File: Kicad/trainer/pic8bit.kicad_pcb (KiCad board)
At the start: 2 copper layers, 160 x 100 mm, 119 parts, among them K101 AC/DC 9-12V, K102 AC/DC 9-12V, K103 PE-450-4X6X-BLACK, K201 MCU 1, K202 MCU 2, K203 ICSP, K204 VIN, K205 VIN, K206 VDD, K207 GND, K208 VDD, K209 GND, K210 HARWIN-254-F-1X10-VERTICAL, K301 I2C/GPIO, K302 I2C/SPI, K303 SPI/GPIO, K304 EUSART/TTL, K401 HARWIN-254-F-1X10-VERTICAL, K402 HARWIN-254-F-1X10-VERTICAL, K409 HARWIN-254-F-1X16-VERTICAL, P401 AN1, P402 AN2, U101 KEYSTONE-24283, U102 KEYSTONE-24283, U103 KEYSTONE-24283, U104 KEYSTONE-24283, U105 NCP5662-ADJ, U201 PIC16F/18F, X101 3M-SJ5376, X102 3M-SJ5376, X103 3M-SJ5376, X104 3M-SJ5376, X105 3M-SJ5376, X201 XTAL-DIL08

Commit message: Up
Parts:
- R401: footprint tronixio:PIHER-PT10LV -> tronixio:PIHER-PT10MV
- U101, U102, U103, U104: value KEYSTONE-24283 -> 24283
- U201: footprint tronixio:DIP-28-W762-SOCKET -> tronixio:DIP-28-W762
- moved S201 0.81 mm to (191.0, 142.0)
- turned S403 to 180 degrees
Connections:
- net VDD renamed +VDD
- net VIN renamed +VIN
- S403 pad 4: GND -> /HID/S5
- S403 pad 5: /HID/S5 -> GND
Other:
- board text removed: "Reset"

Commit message: Up
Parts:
- moved S101 0.25 mm to (88.8, 51.0)
- moved R101 0.20 mm to (103.5, 50.8)
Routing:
- net /HID/S4: track 64.3 -> 65.0 mm
- net /HID/S3: track 85.3 -> 86.0 mm
- net /HID/S1: track 125.4 -> 126.1 mm
- net /HID/S2: track 105.4 -> 106.2 mm
- net /HID/A: track 40.0 -> 40.7 mm
- net Net-(JP401-Pad1): track 15.7 -> 16.4 mm
- net /HID/B: track 37.5 -> 38.2 mm

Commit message: Update
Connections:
- X201 pad 2: GND -> unconnected-(X201-Pad2)
- X201 pad 4: Net-(K201-Pin_9) -> unconnected-(X201-Pad4)
- X201 pad 6: Net-(K201-Pin_10) -> unconnected-(X201-Pad6)
- X201 pad 7: GND -> unconnected-(X201-Pad7)
- X201 pad 8: GND -> unconnected-(X201-Pad8)

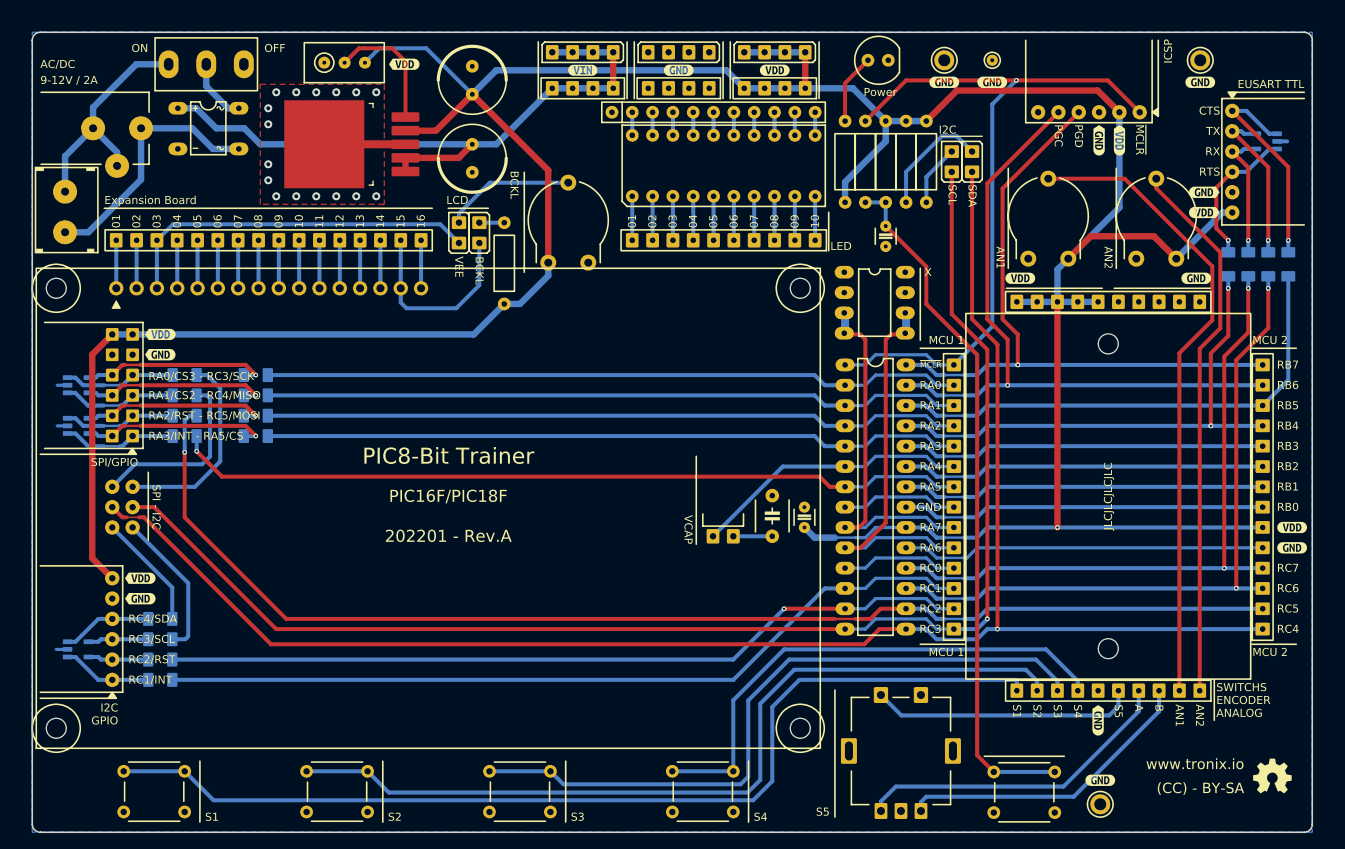
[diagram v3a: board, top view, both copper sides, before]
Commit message: Update Trainer Kicad 8
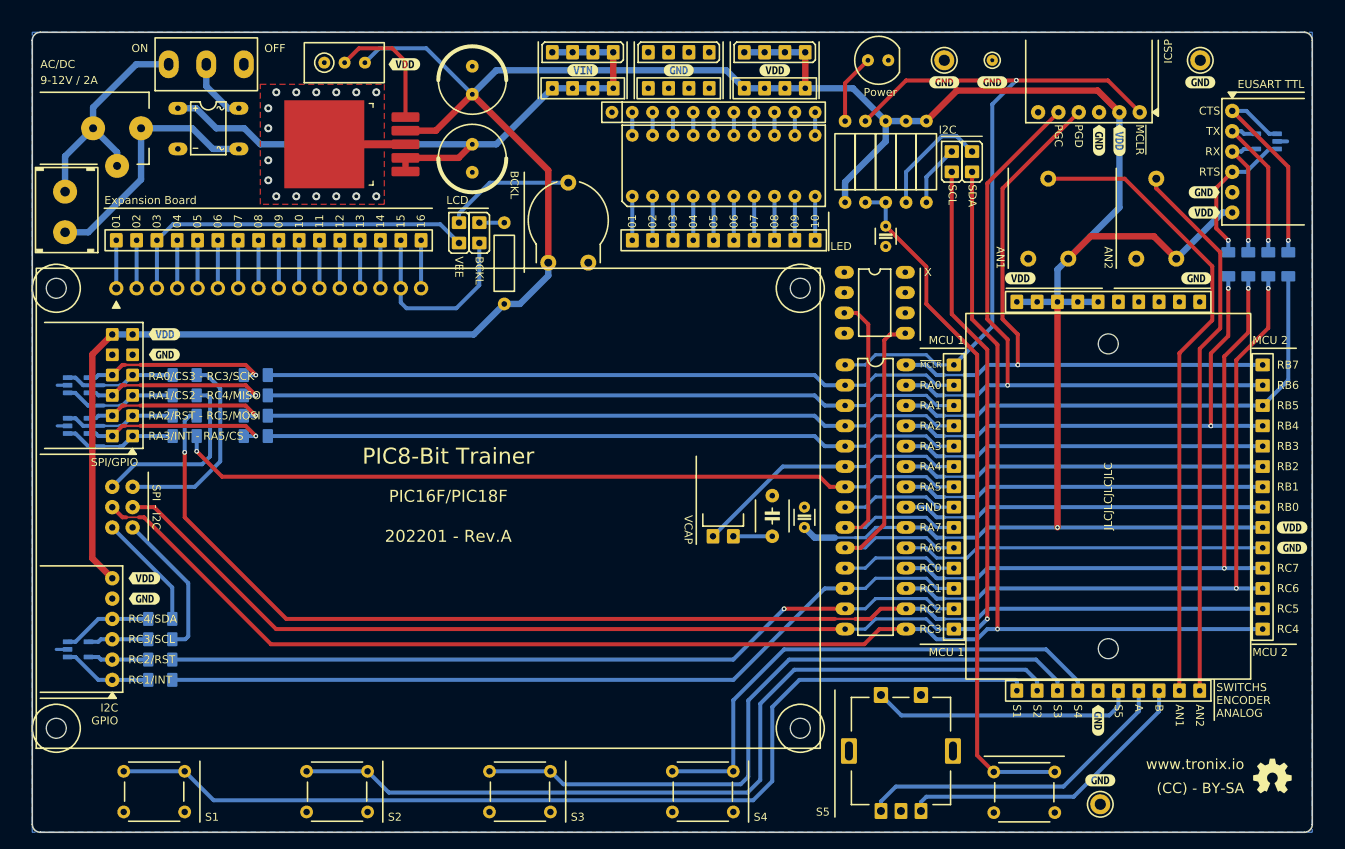
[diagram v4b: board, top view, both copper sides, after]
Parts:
- removed kibuzzard-62A777FA (x7): G***, kibuzzard-62A777FA
- removed kibuzzard-62A77857: G***, kibuzzard-62A77857
- removed kibuzzard-62A778D1 (x2): G***, kibuzzard-62A778D1
- removed kibuzzard-62A778F0: G***, kibuzzard-62A778F0
- removed kibuzzard-62A77FCE: G***, kibuzzard-62A77FCE
- removed kibuzzard-62A77FF4: G***, kibuzzard-62A77FF4
- removed kibuzzard-62A78037: G***, kibuzzard-62A78037
- removed kibuzzard-62A78078: G***, kibuzzard-62A78078
- removed kibuzzard-62A780A0 (x2): G***, kibuzzard-62A780A0
- removed kibuzzard-62A780B6: G***, kibuzzard-62A780B6
- removed kibuzzard-62AA3F24: G***, kibuzzard-62AA3F24
- removed kibuzzard-62ACBAD0: G***, kibuzzard-62ACBAD0
- removed kibuzzard-62ACDA78: G***, kibuzzard-62ACDA78
- added kibuzzard-65F60515: G***, kibuzzard-65F60515, F.Cu at (113.5, 51.0)
- added kibuzzard-65F60520: G***, kibuzzard-65F60520, F.Cu at (135.8, 51.8)
- added kibuzzard-65F6052C: G***, kibuzzard-65F6052C, F.Cu at (147.8, 51.8)
- added kibuzzard-65F60537: G***, kibuzzard-65F60537, F.Cu at (159.8, 51.8)
- added kibuzzard-65F60546: G***, kibuzzard-65F60546, F.Cu at (181.0, 53.2)
- added kibuzzard-65F60553: G***, kibuzzard-65F60553, F.Cu at (187.0, 53.2)
- added kibuzzard-65F60562: G***, kibuzzard-65F60562, F.Cu at (200.3, 60.5)
- added kibuzzard-65F6056F: G***, kibuzzard-65F6056F, F.Cu at (202.9, 60.5)
- added kibuzzard-65F60578: G***, kibuzzard-65F60578, F.Cu at (213.0, 53.2)
- added kibuzzard-65F60585: G***, kibuzzard-65F60585, F.Cu at (213.5, 67.0)
- added kibuzzard-65F60590: G***, kibuzzard-65F60590, F.Cu at (213.5, 69.5)
- added kibuzzard-65F6059C: G***, kibuzzard-65F6059C, F.Cu at (212.5, 77.8)
- added kibuzzard-65F605A7: G***, kibuzzard-65F605A7, F.Cu at (190.5, 77.8)
- added kibuzzard-65F605B3: G***, kibuzzard-65F605B3, F.Cu at (224.5, 108.9)
- added kibuzzard-65F605BE: G***, kibuzzard-65F605BE, F.Cu at (224.5, 111.4)
- added kibuzzard-65F605CA: G***, kibuzzard-65F605CA, F.Cu at (200.2, 133.0)
- added kibuzzard-65F605D7: G***, kibuzzard-65F605D7, F.Cu at (200.5, 140.5)
- added kibuzzard-65F605E6: G***, kibuzzard-65F605E6, F.Cu at (81.0, 117.8)
- added kibuzzard-65F605F2: G***, kibuzzard-65F605F2, F.Cu at (81.0, 115.2)
- added kibuzzard-65F60603: G***, kibuzzard-65F60603, F.Cu at (83.5, 87.3)
- added kibuzzard-65F60610: G***, kibuzzard-65F60610, F.Cu at (83.5, 84.8)
- LED101: footprint tronixio:LED-TH-05MM -> tronixio:LED-TH-ROUND-05MM
- U101, U102, U103, U104: value 24283 -> KEYSTONE-24283
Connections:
- net +VDD renamed POWER-VDD
- net +VIN renamed POWER-VIN
- net GND renamed POWER-GND
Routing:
- net Net-(K201-Pin_10): track 49.3 -> 46.8 mm

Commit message: Update Trainer
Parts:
- moved kibuzzard-65F60515 0.25 mm to (113.8, 51.0)
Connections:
- X201 pad 2: unconnected-(X201-Pad2) -> POWER-GND
- X201 pad 4: unconnected-(X201-Pad4) -> Net-(K201-Pin_9)
- X201 pad 6: unconnected-(X201-Pad6) -> Net-(K201-Pin_10)
- X201 pad 7: unconnected-(X201-Pad7) -> POWER-GND
- X201 pad 8: unconnected-(X201-Pad8) -> POWER-GND
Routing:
- net POWER-GND: track 75.7 -> 70.4 mm
- net Net-(K201-Pin_10): track 46.8 -> 49.2 mm
- net POWER-VDD: track 405.2 -> 405.9 mm

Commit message: Update
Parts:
- U201: footprint tronixio:DIP-28-W762 -> tronixio:DIP-28-W762-SOCKET

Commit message: Up
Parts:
- U101, U102, U103, U104: value KEYSTONE-24283 -> 24283
- U105: footprint tronixio:TO-263-5 -> tronixio:TO-263-5-TABPIN3
- U201: footprint tronixio:DIP-28-W762-SOCKET -> tronixio:DIP-28-W762
- turned U105 to 180 degrees

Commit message: Up
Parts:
- K101: footprint tronixio:CUI-PJ-102AH -> tronixio:SSD-PJ-102AH
- K210: value HARWIN-254-F-1X10-VERTICAL -> VDD & GND
- K401: value HARWIN-254-F-1X10-VERTICAL -> LED ARRAY
- K402: value HARWIN-254-F-1X10-VERTICAL -> SWITCH, ENCODER & ANALOG
- K409: value HARWIN-254-F-1X16-VERTICAL -> EXPANSION BOARD
- U101, U102, U103, U104: value 24283 -> KEYSTONE-24283
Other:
- outline, holes or cut-outs redrawn
